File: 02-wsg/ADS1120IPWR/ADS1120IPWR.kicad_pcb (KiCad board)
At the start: 2 copper layers, 1 part, among them U1 ADS1120IPWR

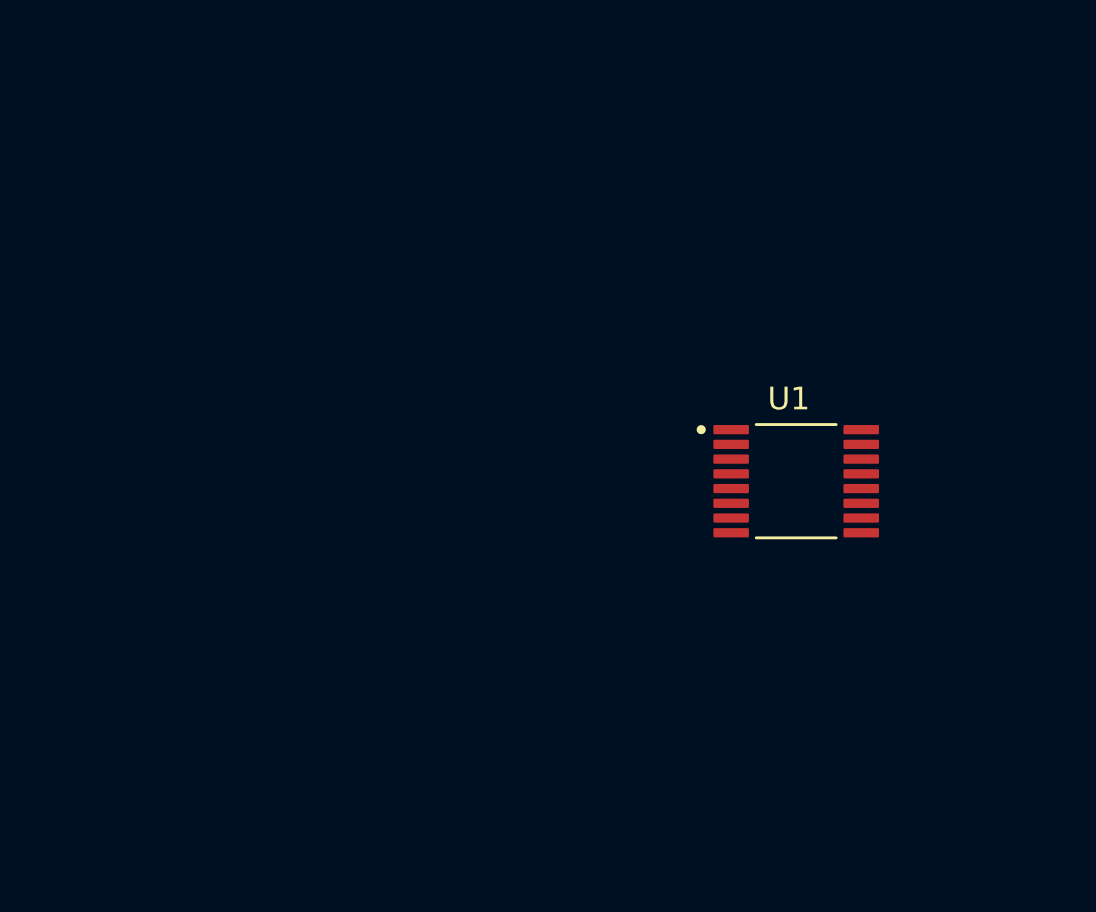
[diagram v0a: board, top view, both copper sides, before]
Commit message: adc initial schematic
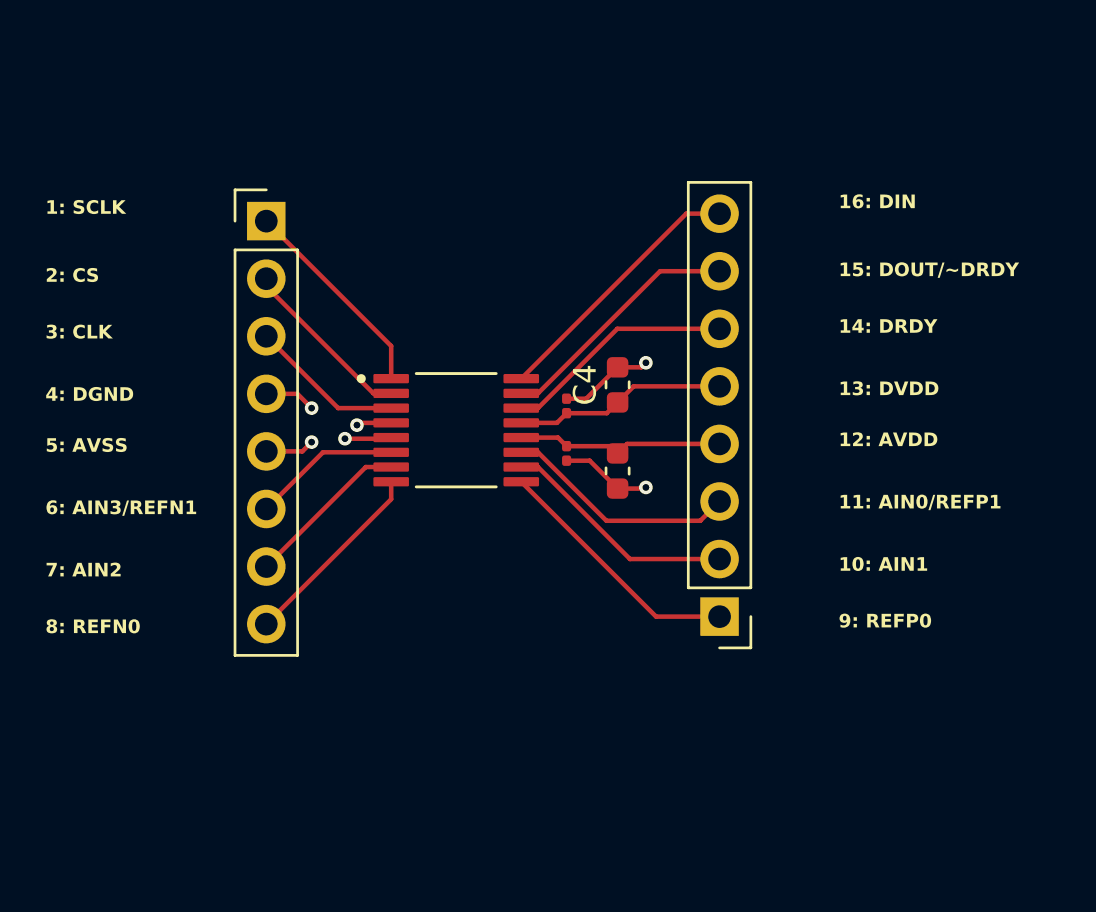
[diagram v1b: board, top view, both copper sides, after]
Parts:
- added C1: 0.1 μF, Capacitor_SMD:C_0201_0603Metric, F.Cu at (157.8, 65.5)
- added C2: 10 μF, Capacitor_SMD:C_0603_1608Metric, F.Cu at (160.0, 66.3)
- added C3: 0.1 μF, Capacitor_SMD:C_0201_0603Metric, F.Cu at (157.8, 63.4)
- added C4: 10 μF, Capacitor_SMD:C_0603_1608Metric, F.Cu at (160.0, 62.5)
- added J1: Conn_01x08, Connector_PinHeader_2.54mm:PinHeader_1x08_P2.54mm_Vertical, F.Cu at (144.5, 55.2)
- added J2: Conn_01x08, Connector_PinHeader_2.54mm:PinHeader_1x08_P2.54mm_Vertical, F.Cu at (164.5, 72.7)
- moved U1 15.2 mm to (152.9, 64.5)
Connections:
- U1 pad 1: unconnected-(U1-SCLK-Pad1) -> SCLK
- U1 pad 10: unconnected-(U1-AIN1-Pad10) -> AIN1
- U1 pad 11: unconnected-(U1-AIN0/REFP1-Pad11) -> AIN0/REFP1
- U1 pad 12: unconnected-(U1-AVDD-Pad12) -> AVDD
- U1 pad 13: unconnected-(U1-DVDD-Pad13) -> DVDD
- U1 pad 14: unconnected-(U1-~{DRDY}-Pad14) -> DRDY
- U1 pad 15: unconnected-(U1-DOUT/~DRDY-Pad15) -> DOUT
- U1 pad 16: unconnected-(U1-DIN-Pad16) -> DIN
- U1 pad 2: unconnected-(U1-~{CS}-Pad2) -> CS
- U1 pad 3: unconnected-(U1-CLK-Pad3) -> CLK
- U1 pad 4: unconnected-(U1-DGND-Pad4) -> DGND
- U1 pad 5: unconnected-(U1-AVSS-Pad5) -> AVSS
- U1 pad 6: unconnected-(U1-AIN3/REFN1-Pad6) -> AIN3/REFN1
- U1 pad 7: unconnected-(U1-AIN2-Pad7) -> AIN2
- U1 pad 8: unconnected-(U1-REFN0-Pad8) -> REFN0
- U1 pad 9: unconnected-(U1-REFP0-Pad9) -> REFP0
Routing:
- net DIN: track 0.00 -> 11.8 mm
- net REFP0: track 0.00 -> 11.2 mm
- net DOUT: track 0.00 -> 11.0 mm
- net AIN1: track 0.00 -> 10.4 mm
- net AIN0/REFP1: track 0.00 -> 10.4 mm
- net DRDY: track 0.00 -> 10.2 mm
- net DVDD: track 0.00 -> 9.42 mm
- net SCLK: track 0.00 -> 9.23 mm
- net AVDD: track 0.00 -> 9.21 mm
- net REFN0: track 0.00 -> 8.56 mm
- net AVSS: track 0.00 -> 8.51 mm, vias 0 -> 3
- net DGND: track 0.00 -> 7.97 mm, vias 0 -> 3
- net CS: track 0.00 -> 7.80 mm
- net AIN2: track 0.00 -> 7.33 mm
- net CLK: track 0.00 -> 6.82 mm
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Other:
- board text added: "10: AIN1"
- board text added: "11: AIN0/REFP1"
- board text added: "12: AVDD"
- board text added: "13: DVDD"
- board text added: "14: DRDY"
- board text added: "15: DOUT/~DRDY"
- board text added: "16: DIN"
- board text added: "1: SCLK"
- board text added: "2: CS"
- board text added: "3: CLK"
- board text added: "4: DGND"
- board text added: "5: AVSS"
- board text added: "6: AIN3/REFN1"
- board text added: "7: AIN2"
- board text added: "8: REFN0"
- board text added: "9: REFP0"

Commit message: updated board
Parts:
- added G***: BJR_LOGO, Library:BJR_LOGO, F.Cu at (155.0, 54.2)
- added G***: BJR_LOGO, Library:BJR_LOGO, B.Cu at (155.0, 54.2)
- moved J2 1.54 mm to (166.0, 73.0)
- moved C3 1.27 mm to (159.0, 63.2)
- moved C1 1.25 mm to (159.0, 65.6)
- moved J1 0.96 mm to (145.5, 55.3)
- moved U1 0.96 mm to (153.8, 64.6)
- moved C4 0.80 mm to (160.8, 62.8)
- moved C2 0.79 mm to (160.8, 66.0)
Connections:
- net AVSS renamed GND
- net CS renamed CS!
- net DGND renamed GNDD
- net DRDY renamed DRDY!
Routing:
- net GND: track 8.51 -> 4.83 mm, vias 3 -> 4
- net AIN1: track 10.4 -> 11.4 mm
- net REFP0: track 11.2 -> 12.1 mm
- net GNDD: track 7.97 -> 7.27 mm, vias 3 -> 4
- net DVDD: track 9.42 -> 10.1 mm
- net DRDY!: track 10.2 -> 10.8 mm
- net DOUT: track 11.0 -> 11.6 mm
- net DIN: track 11.8 -> 12.4 mm
- net AVDD: track 9.21 -> 9.79 mm
- added copper zone on B.Cu, net GNDD
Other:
- board outline added: 26.5 x 24.5 mm
- board text added: "10: AIN1 *AVSS-0.1~AVDD+0.1v"
- board text added: "11: AIN0/REFP1 *AVSS-0.1~AVDD+0.1v"
- board text added: "12: AVDD *to AVSS: 2.3~5.5v *to DGND: 2.3~2.75v"
- board text added: "13: DVDD *to DGND: 2.3~5.5v"
- board text added: "14: DRDY! *active low"
- board text added: "15: DOUT /~DRDY!"
- board text added: "2: CS! *active low"
- board text added: "5: AVSS *unipolar to DGND -0.1~0.1v *bipolar to DGND -2.75~-2.3v"
- board text added: "6: AIN3/REFN1 *AVSS-0.1~AVDD+0.1v"
- board text added: "7: AIN2 *AVSS-0.1~AVDD+0.1v"
- board text added: "8: REFN0 *AVSS-0.1~AVDD+0.1v"
- board text added: "9: REFP0 *AVSS-0.1~AVDD+0.1v"
- board text added: "Blue Jay Racing @ JHU 22XT WSG ADC Breakout Shuwen Zheng Emma Ouyang"
- board text removed: "10: AIN1"
- board text removed: "11: AIN0/REFP1"
- board text removed: "12: AVDD"
- board text removed: "13: DVDD"
- board text removed: "14: DRDY"
- board text removed: "15: DOUT/~DRDY"
- board text removed: "2: CS"
- board text removed: "5: AVSS"
- board text removed: "6: AIN3/REFN1"
- board text removed: "7: AIN2"
- board text removed: "8: REFN0"
- board text removed: "9: REFP0"

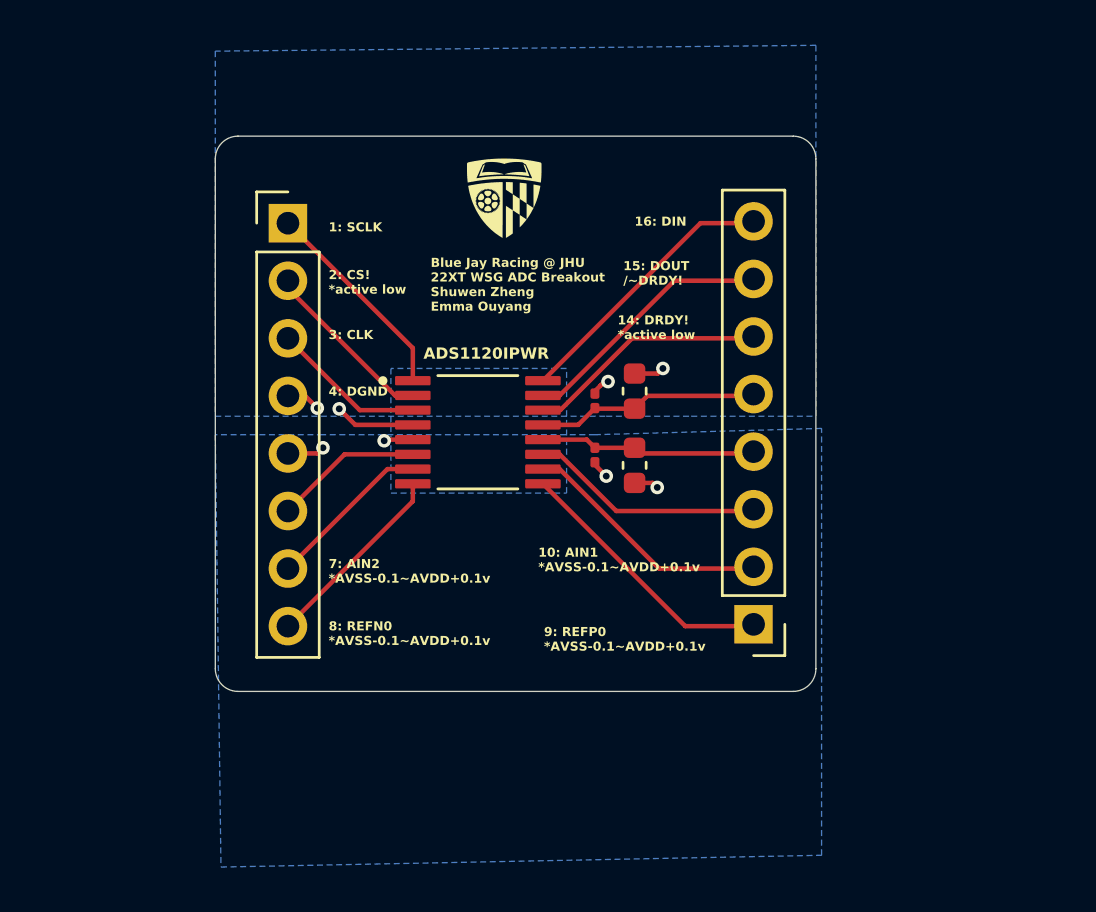
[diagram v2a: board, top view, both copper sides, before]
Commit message: Changed WSG ADC breakout board size
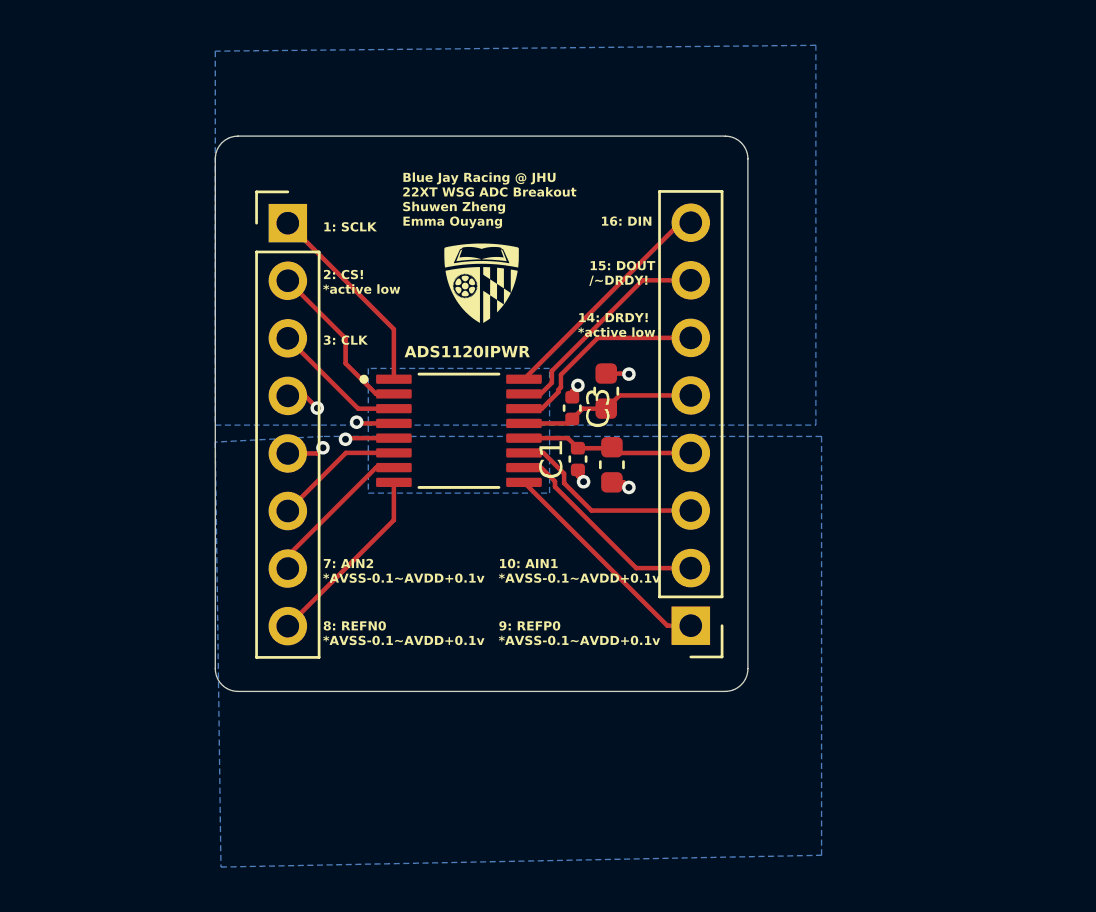
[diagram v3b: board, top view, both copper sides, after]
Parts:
- C1, C3: footprint Capacitor_SMD:C_0201_0603Metric -> Capacitor_SMD:C_0402_1005Metric
- moved G*** 3.88 mm to (154.0, 58.0)
- moved J2 2.77 mm to (163.2, 73.1)
- moved C4 1.25 mm to (159.5, 62.8)
- moved G*** 1.12 mm to (154.0, 54.8)
- moved C3 1.05 mm to (158.0, 63.5)
- moved C2 1.00 mm to (159.8, 66.0)
- moved U1 0.84 mm to (153.0, 64.5)
- moved C1 0.77 mm to (158.2, 65.8)
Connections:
- C3 pad 1: GNDD -> GND
- C4 pad 2: GNDD -> GND
- J1 pad 4: GNDD -> GND
- U1 pad 4: GNDD -> GND
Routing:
- net GNDD: track 7.27 -> 0.00 mm, vias 4 -> 0
- net GND: track 4.83 -> 10.1 mm, vias 4 -> 8
- net DVDD: track 10.1 -> 7.87 mm
- net DIN: track 12.4 -> 10.2 mm
- net REFP0: track 12.1 -> 9.98 mm
- net AVDD: track 9.79 -> 7.67 mm
- net AIN1: track 11.4 -> 9.33 mm
- net AIN0/REFP1: track 10.6 -> 8.66 mm
- net DOUT: track 11.6 -> 9.74 mm
- net DRDY!: track 10.8 -> 9.04 mm
- net CLK: track 6.82 -> 5.97 mm
- net AIN3/REFN1: track 6.55 -> 5.74 mm
- added copper zone on B.Cu, net GND
- removed copper zone on B.Cu, net GNDD
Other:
- board size 26.5 x 24.5 mm -> 23.5 x 24.5 mm

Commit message: Added second ground plane to ADS1120 breakout
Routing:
- net GND: vias 8 -> 12
- added copper zone on F.Cu, net GND
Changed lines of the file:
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@@
 			(pintype "power_in")
 			(solder_mask_margin 0.102)
+			(zone_connect 1)
 		)
 		(pad "5" smd roundrect
@@
 	)
 	(via
+		(at 149 54.5)
+		(size 0.5)
+		(drill 0.3)
+		(layers "F.Cu" "B.Cu")
+		(net 2)
+	)
+	(via
 		(at 147.996062 64.875298)
 		(size 0.6)
@@
 	)
 	(via
+		(at 150 72)
+		(size 0.5)
+		(drill 0.3)
+		(layers "F.Cu" "B.Cu")
+		(net 2)
+	)
+	(via
 		(at 158.25 62.5)
 		(size 0.6)
@@
 	(via
 		(at 146.75 63.5)
-		(size 0.6)
+		(size 0.5)
+		(drill 0.3)
+		(layers "F.Cu" "B.Cu")
+		(net 2)
+	)
+	(via
+		(at 155.5 54.5)
+		(size 0.5)
 		(drill 0.3)
 		(layers "F.Cu" "B.Cu")
@@
 		(net 2)
 	)
+	(via
+		(at 156.5 72)
+		(size 0.5)
+		(drill 0.3)
+		(layers "F.Cu" "B.Cu")
+		(net 2)
+	)
 	(segment
 		(start 160.085 62.94)
@@
 		(net 2)
 		(net_name "GND")
-		(layer "B.Cu")
+		(layers "F.Cu" "B.Cu")
 		(hatch edge 0.5)
 		(priority 1)
@@
 		(net 2)
 		(net_name "GND")
-		(layer "B.Cu")
+		(layers "F.Cu" "B.Cu")
 		(hatch edge 0.5)
 		(connect_pads
@@
 		(polygon
 			(pts
-				(xy 147 64.75) (xy 142.25 65) (xy 142.5 83.75) (xy 169 83.230392) (xy 169 64.75) (xy 158.75 64.75)
+				(xy 146.9 64.5) (xy 142.25 64.6) (xy 142.5 83.75) (xy 169 83.230392) (xy 169 64.75) (xy 158.75 64.75)
 			)
 		)
@@
 		(net 2)
 		(net_name "GND")
-		(layer "B.Cu")
+		(layers "F.Cu" "B.Cu")
 		(hatch edge 0.5)
 		(priority 2)
